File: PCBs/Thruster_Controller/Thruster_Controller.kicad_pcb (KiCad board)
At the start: 4 copper layers, 36 x 37.5 mm, 111 parts, among them J1 PHASE_A, J2 PHASE_B, J3 PHASE_C, J4 Conn_01x01, J5 Pogo Conn, J6 Conn_01x01, J7 Conn_01x01, J8 Conn_01x01, Q1 SIZF906DT, Q2 SIZF906DT, Q3 SIZF906DT, U1 DRV8305, U2 RTQ2569-50GQW, U3 MCP2515, U4 TPS62172DSGR, U5 TMS320F28027F, U8 MCP2562, Y1 20MHz

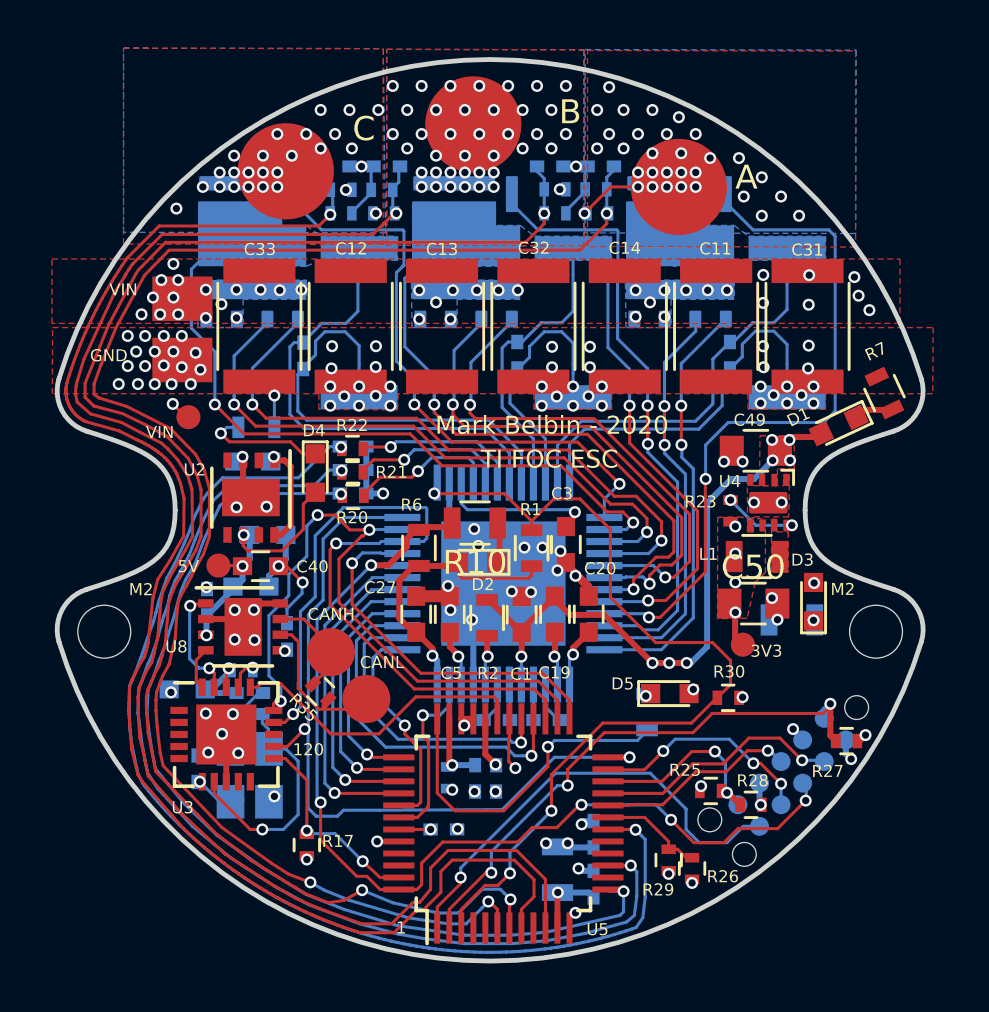
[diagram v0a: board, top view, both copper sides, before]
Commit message: Changed Cap Bank + Gerbers
- Changed cap bank to 3 aluminum poly caps plus 3 ceramic caps
- Fixed routing
- Generated Gerbers
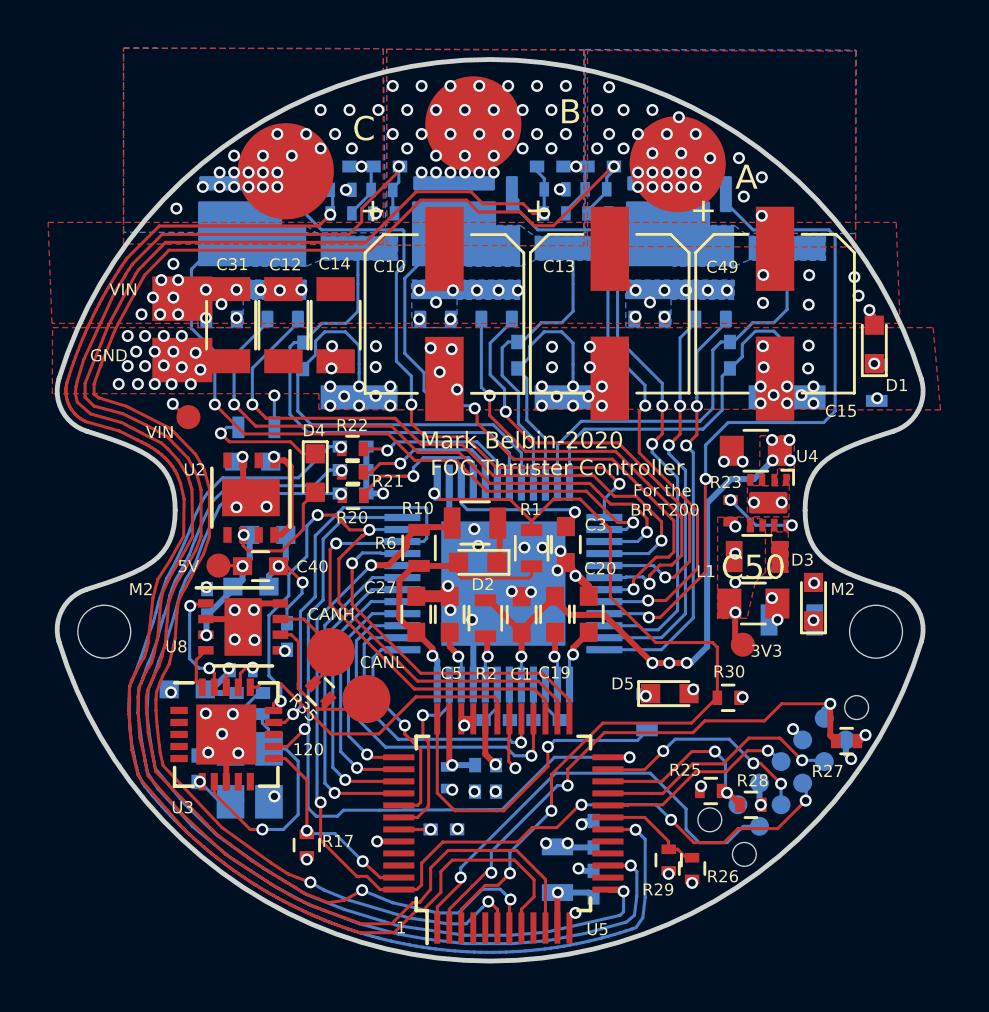
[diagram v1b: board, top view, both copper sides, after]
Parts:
- removed C11, C32, C33: 22uF, Capacitors_SMD:C_1812
- added C10: 22uF, Capacitors_SMD:CP_Elec_6.3x5.8, F.Cu at (97.5, 91.3)
- added C15: 22uF, Capacitors_SMD:CP_Elec_6.3x5.8, F.Cu at (111.3, 91.3)
- C12, C14, C31: footprint Capacitors_SMD:C_1812 -> Capacitors_SMD:C_1206
- C13: footprint Capacitors_SMD:C_1812 -> Capacitors_SMD:CP_Elec_6.3x5.8
- R7: moved to B.Cu
- moved C31 24.0 mm to (88.7, 91.8)
- moved C14 12.0 mm to (93.0, 91.8)
- moved C13 6.99 mm to (104.4, 91.3)
- moved D1 3.69 mm to (115.4, 92.5), turned to 90 degrees
- moved C12 2.80 mm to (90.8, 91.8)
- moved J1 0.95 mm to (107.2, 85.0)
- moved R7 0.53 mm to (115.5, 94.2), turned to 270 degrees
- moved R2 0.08 mm to (99.2, 103.9)
- turned R5 to 180 degrees
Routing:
- net /Powertrain/Phase_A: track 2.68 -> 0.00 mm, vias 31 -> 27
- net /TI_MCU/ADCINA7: track 63.9 -> 65.9 mm
- net /Powertrain/SH_B: track 21.4 -> 19.6 mm
- net /Powertrain/GH_B: track 21.6 -> 20.0 mm
- net /TI_MCU/ADCINA0: track 61.7 -> 63.3 mm
- net Net-(D1-Pad1): track 1.63 -> 0.12 mm, vias 0 -> 1
- net +BATT: track 32.8 -> 34.0 mm, vias 50 -> 51
- net /Powertrain/GL_C: track 24.9 -> 25.6 mm
- net GND: track 63.2 -> 63.6 mm, vias 106 -> 111
- net /Powertrain/Phase_B: vias 39 -> 33
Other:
- board text added: "FOC Thruster Controller"
- board text added: "For the BR T200"
- board text added: "Mark Belbin-2020"
- board text removed: "Mark Belbin - 2020"
- board text removed: "TI FOC ESC"
